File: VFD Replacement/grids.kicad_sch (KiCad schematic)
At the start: 6 parts, among them Q1 MMDT2222A, Q2 MMDT2222A, Q3 MMDT2222A, Q4 MMDT2222A, Q5 MMDT2222A, Q6 MMDT2222A

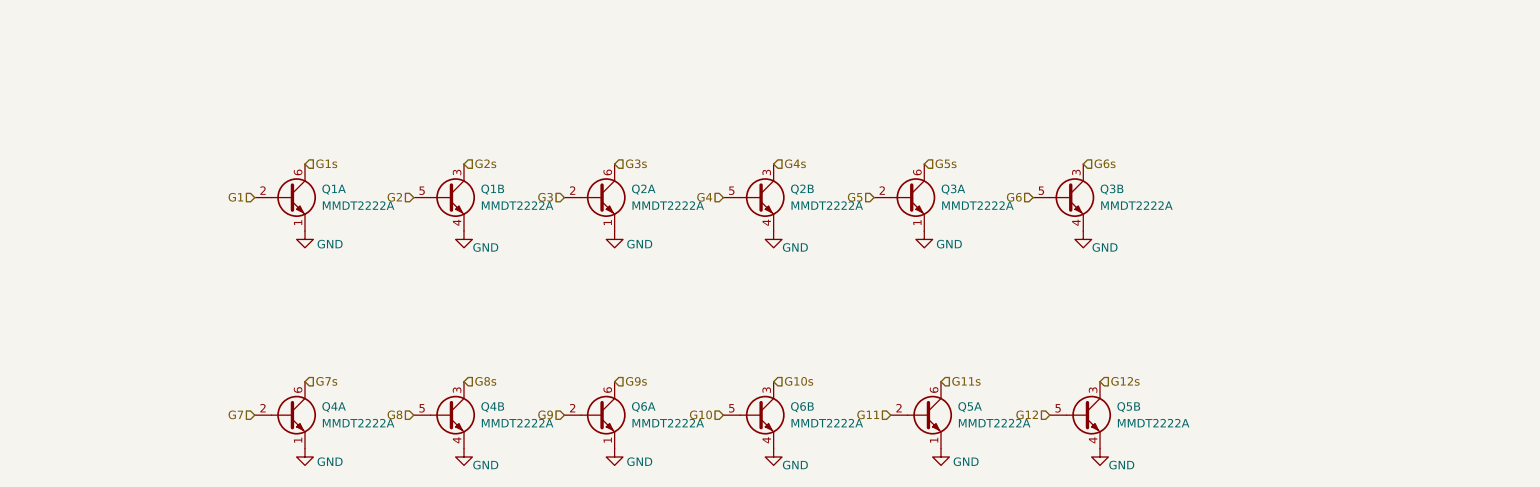
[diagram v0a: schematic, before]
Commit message: Update VFD Replacement layout
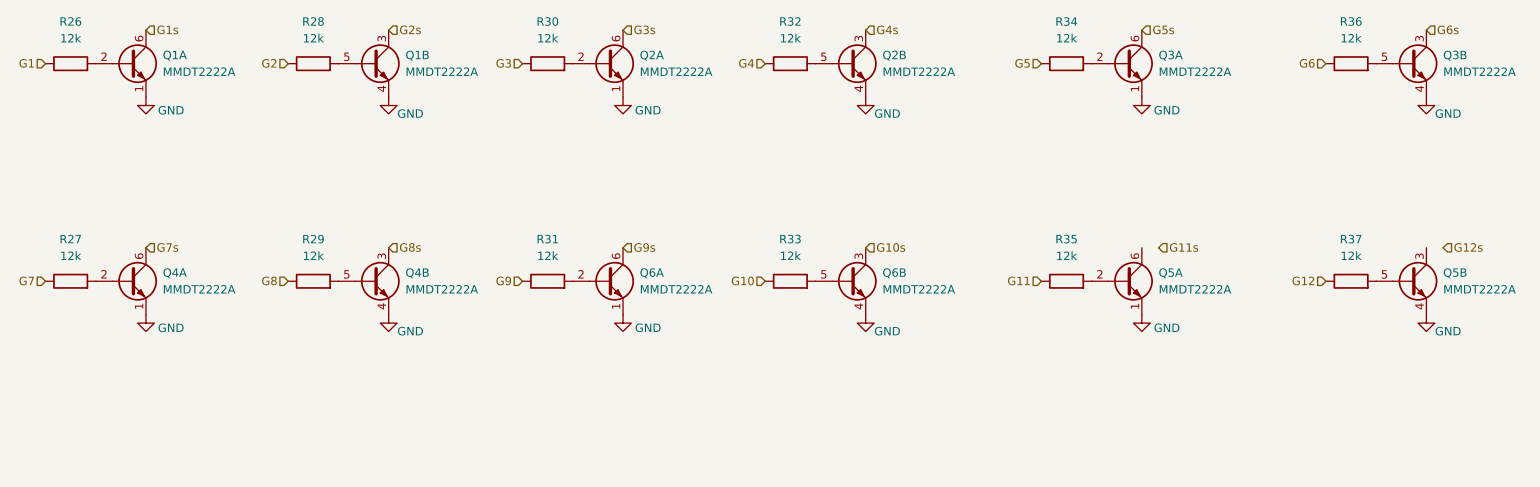
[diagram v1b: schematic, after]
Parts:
- added R26, R27, R28, R29, R30, R31, R32, R33, R34, R35, R36, R37: 12k, Resistor_SMD:R_0603_1608Metric_Pad0.98x0.95mm_HandSolder, symbol Device:R
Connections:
- net G1: now also R26.1; no longer Q1.2 (B1)
- net G10: now also R33.1; no longer Q6.5 (B2)
- net G11: now also R35.1; no longer Q5.2 (B1)
- net G11s: no longer Q5.6 (C1)
- net G12: now also R37.1; no longer Q5.5 (B2)
- net G12s: no longer Q5.3 (C2)
- net G2: now also R28.1; no longer Q1.5 (B2)
- net G3: now also R30.1; no longer Q2.2 (B1)
- net G4: now also R32.1; no longer Q2.5 (B2)
- net G5: now also R34.1; no longer Q3.2 (B1)
- net G6: now also R36.1; no longer Q3.5 (B2)
- net G7: now also R27.1; no longer Q4.2 (B1)
- net G8: now also R29.1; no longer Q4.5 (B2)
- net G9: now also R31.1; no longer Q6.2 (B1)
- new net: Q2.5 (B2), R32.2
- new net: Q1.5 (B2), R28.2
- new net: Q4.5 (B2), R29.2
- new net: Q6.2 (B1), R31.2
- new net: Q6.5 (B2), R33.2
- new net: Q3.2 (B1), R34.2
- new net: Q3.5 (B2), R36.2
- new net: Q1.2 (B1), R26.2
- new net: Q5.2 (B1), R35.2
- new net: Q2.2 (B1), R30.2
- new net: Q4.2 (B1), R27.2
- new net: Q5.5 (B2), R37.2
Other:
- moved on the sheet: Q1A, Q1B, Q2A, Q2B, Q3A, Q3B, Q4A, Q4B, Q5A, Q5B, Q6A, Q6B

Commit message: Complete
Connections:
- net G11s: now also Q5.6 (C1)
- net G12s: now also Q5.3 (C2)
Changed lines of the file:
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@@
     (effects (font (size 1.27 1.27)) (justify right))
   )
-  (hierarchical_label "G11s" (shape input) (at 207.01 95.25 0) (fields_autoplaced)
+  (hierarchical_label "G11s" (shape input) (at 204.47 95.25 0) (fields_autoplaced)
     (effects (font (size 1.27 1.27)) (justify left))
   )
@@
     (effects (font (size 1.27 1.27)) (justify left))
   )
-  (hierarchical_label "G12s" (shape input) (at 250.19 95.25 0) (fields_autoplaced)
+  (hierarchical_label "G12s" (shape input) (at 247.65 95.25 0) (fields_autoplaced)
     (effects (font (size 1.27 1.27)) (justify left))
   )

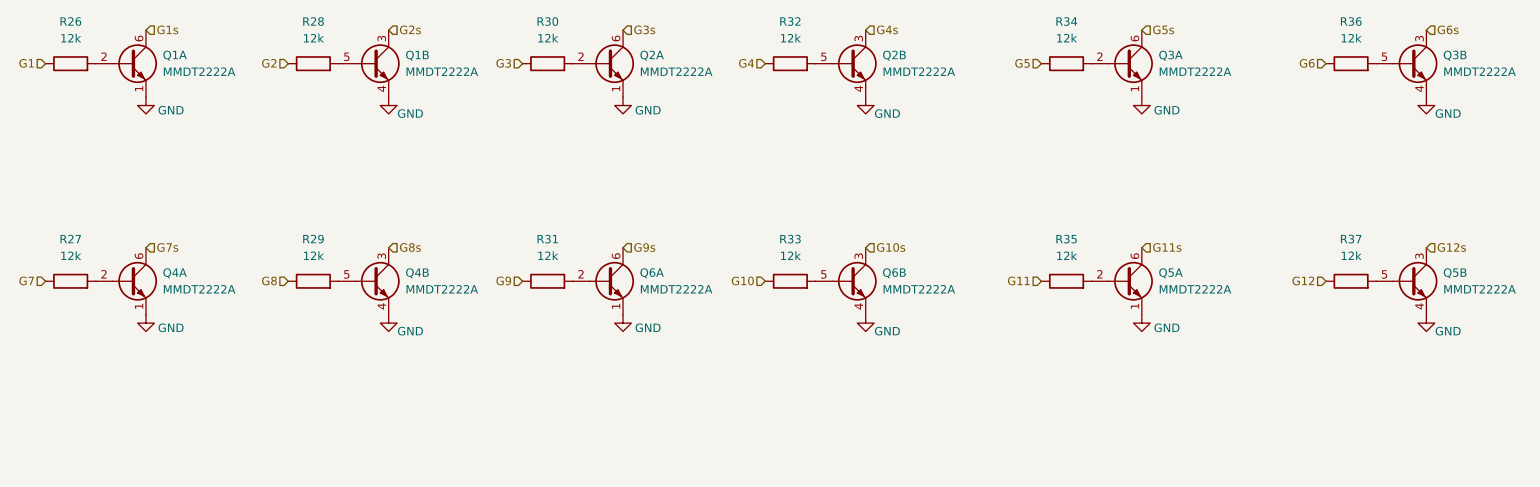
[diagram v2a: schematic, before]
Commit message: Update values from sim
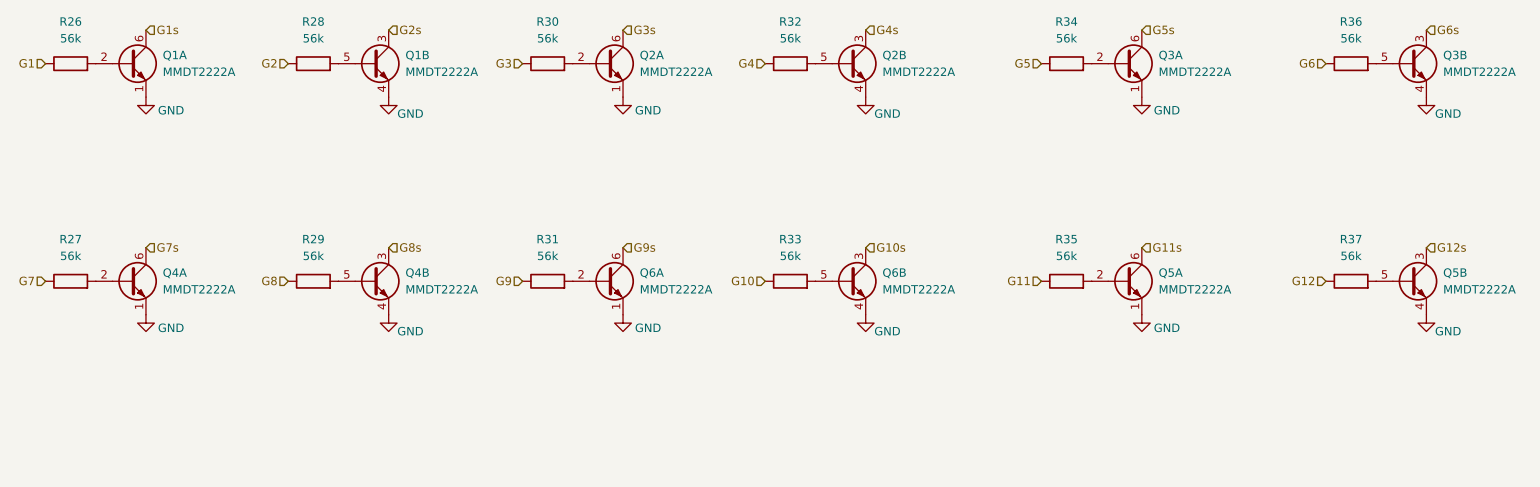
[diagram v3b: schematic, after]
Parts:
- R26, R27, R28, R29, R30, R31, R32, R33, R34, R35, R36, R37: value 12k -> 56k
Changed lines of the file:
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@@
       (effects (font (size 1.27 1.27)))
     )
-    (property "Value" "12k" (at 151.13 63.5 90)
+    (property "Value" "56k" (at 151.13 63.5 90)
       (effects (font (size 1.27 1.27)))
     )
@@
       (effects (font (size 1.27 1.27)))
     )
-    (property "Value" "12k" (at 78.74 63.5 90)
+    (property "Value" "56k" (at 78.74 63.5 90)
       (effects (font (size 1.27 1.27)))
     )
@@
       (effects (font (size 1.27 1.27)))
     )
-    (property "Value" "12k" (at 78.74 96.52 90)
+    (property "Value" "56k" (at 78.74 96.52 90)
       (effects (font (size 1.27 1.27)))
     )
@@
       (effects (font (size 1.27 1.27)))
     )
-    (property "Value" "12k" (at 114.3 96.52 90)
+    (property "Value" "56k" (at 114.3 96.52 90)
       (effects (font (size 1.27 1.27)))
     )
@@
       (effects (font (size 1.27 1.27)))
     )
-    (property "Value" "12k" (at 151.13 96.52 90)
+    (property "Value" "56k" (at 151.13 96.52 90)
       (effects (font (size 1.27 1.27)))
     )
@@
       (effects (font (size 1.27 1.27)))
     )
-    (property "Value" "12k" (at 193.04 63.5 90)
+    (property "Value" "56k" (at 193.04 63.5 90)
       (effects (font (size 1.27 1.27)))
     )
@@
       (effects (font (size 1.27 1.27)))
     )
-    (property "Value" "12k" (at 236.22 63.5 90)
+    (property "Value" "56k" (at 236.22 63.5 90)
       (effects (font (size 1.27 1.27)))
     )
@@
       (effects (font (size 1.27 1.27)))
     )
-    (property "Value" "12k" (at 193.04 96.52 90)
+    (property "Value" "56k" (at 193.04 96.52 90)
       (effects (font (size 1.27 1.27)))
     )
@@
       (effects (font (size 1.27 1.27)))
     )
-    (property "Value" "12k" (at 114.3 63.5 90)
+    (property "Value" "56k" (at 114.3 63.5 90)
       (effects (font (size 1.27 1.27)))
     )
@@
       (effects (font (size 1.27 1.27)))
     )
-    (property "Value" "12k" (at 41.91 63.5 90)
+    (property "Value" "56k" (at 41.91 63.5 90)
       (effects (font (size 1.27 1.27)))
     )
@@
       (effects (font (size 1.27 1.27)))
     )
-    (property "Value" "12k" (at 236.22 96.52 90)
+    (property "Value" "56k" (at 236.22 96.52 90)
       (effects (font (size 1.27 1.27)))
     )
@@
       (effects (font (size 1.27 1.27)))
     )
-    (property "Value" "12k" (at 41.91 96.52 90)
-      (effects (font (size 1.27 1.27)))
-    )
+    (property "Value" "56k" (at 41.91 96.52 90)
+      (effects (font (size 1.27 1.27)))
+    )
